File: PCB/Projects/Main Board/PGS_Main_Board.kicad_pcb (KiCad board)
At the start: 4 copper layers, 109.9 x 60.8 mm, 119 parts, among them J1 SM02B-SURS-TF_LF__SN_, J2 SM02B-SURS-TF_LF__SN_, J3 Molex 505110-0892, J5 Molex 505110-0892, J6 Molex 505110-0492, J7 Molex 505110-0492, J8 Conn_01x04_Pin, J9 Molex 505110-1792, Q1 MMBT2222A, Q2 MMBT2222A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

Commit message: Main Board Update
- Put 1uF caps closer to designated pins
- Update timestamp on PCB mask
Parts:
- C18, C22: value 100nF -> 1uF
- C3, C6: value 1uF -> 100nF
- SW1, SW15, SW16, SW2, SW3, SW4: value TS-1187A-C-A-B -> TS-1187A-C-A-B
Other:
- board text added: "Hand Held Legend, LLC Designed By Mitch Cairns 7.20.2025"
- board text removed: "Hand Held Legend, LLC Designed By Mitch"

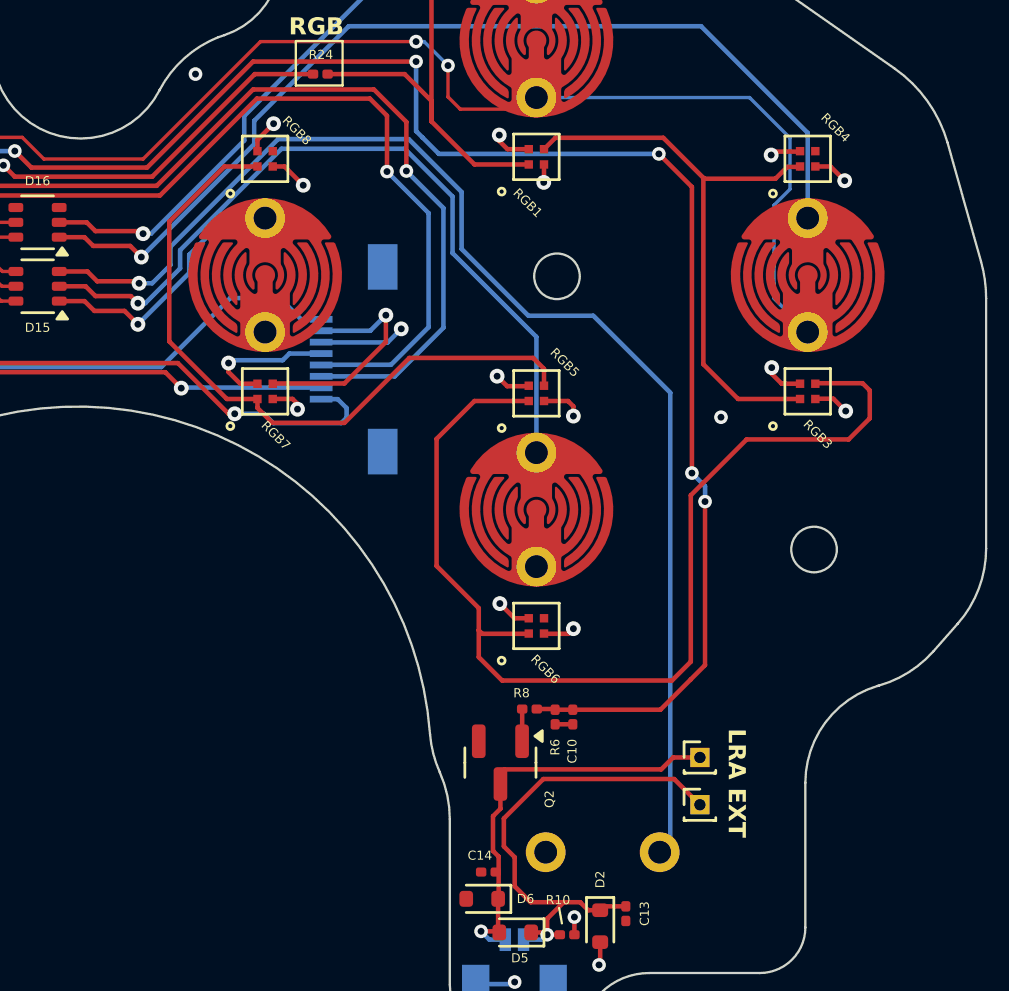
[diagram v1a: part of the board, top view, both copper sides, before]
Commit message: Main Board/Trigger Board Update
- Main board updated with Kailh tactile switches
- Trigger board updated with Kailh tactile switches
- USBW board updated to remove unneeded diode, move position of USB-C port
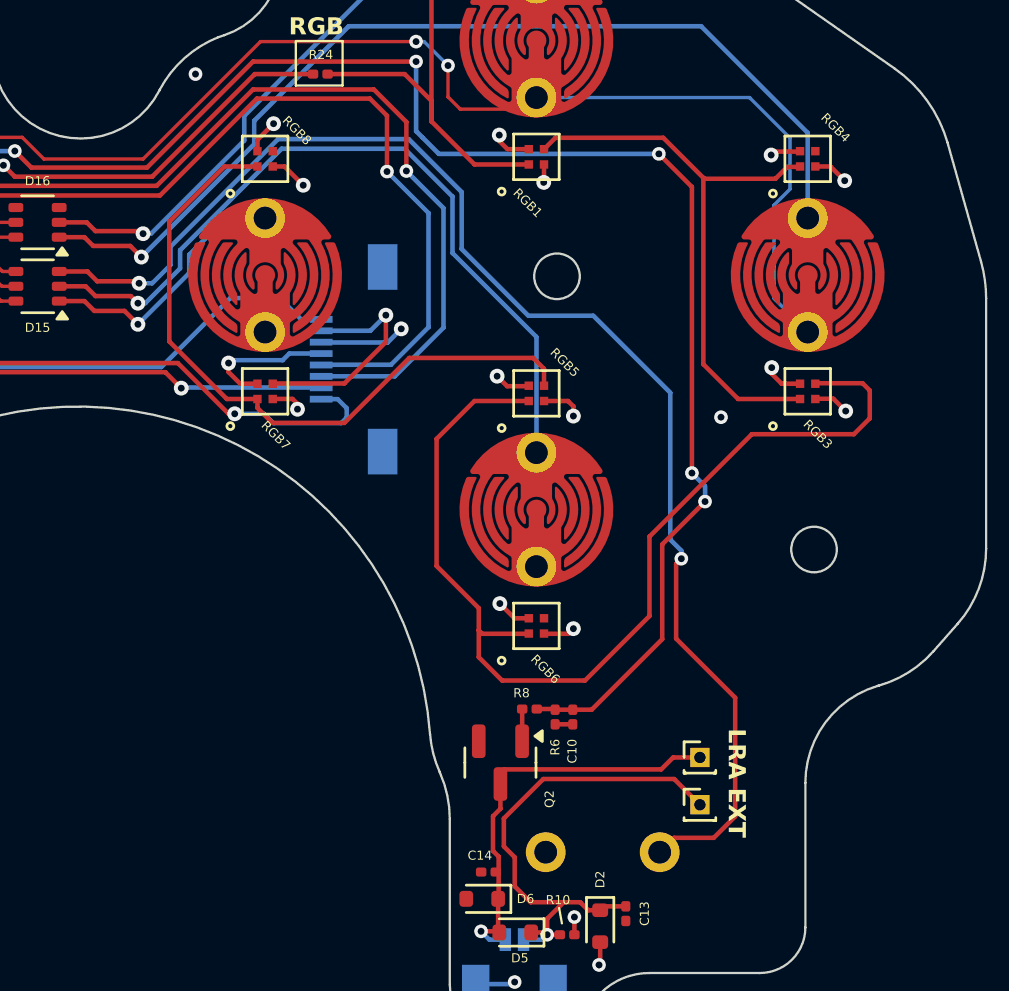
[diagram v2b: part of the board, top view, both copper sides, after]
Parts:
- SW14, SW9: value EVQ-P0E07K -> CMI627301D60
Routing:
- net Net-(D15C-A): track 56.5 -> 60.7 mm, vias 1 -> 2
- net Net-(RGB3-DOUT): track 47.7 -> 45.5 mm
- net LRA_R: track 95.0 -> 93.3 mm
